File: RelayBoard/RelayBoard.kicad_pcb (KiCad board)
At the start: 2 copper layers, 96.3 x 38.1 mm, 63 parts, among them J1 Micro_SD_Card, J10 Conn_01x04_Male, J11 Conn_01x04_Male, J12 Conn_01x04_Male, J2 Screw_Terminal_01x02, J3 Conn_01x04_Male, J4 Conn_01x04_Male, J5 Conn_01x04_Male, J6 Conn_01x04_Male, J7 SI-52008-F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

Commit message: add jlcjlcjlcjlc
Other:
- board text added: "JLCJLCJLCJLC"
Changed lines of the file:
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@@
   (general
     (thickness 1.6)
-    (drawings 10)
+    (drawings 11)
     (tracks 705)
     (zones 0)
@@
       (outputformat 1)
       (mirror false)
-      (drillshape 1)
+      (drillshape 0)
       (scaleselection 1)
       (outputdirectory ""))
@@
     )
   )
+  (gr_text JLCJLCJLCJLC (at 97.79 80.264 -90) (layer F.SilkS)
+    (effects (font (size 1 1) (thickness 0.15)))
+  )
   (gr_text "Relay Board v1 by Clive Chan" (at 167.64 97.282) (layer F.SilkS)

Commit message: Programming connector, CAN connectors 2.54mm
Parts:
- removed J12, J6: Conn_01x04_Male, Connector_PinHeader_1.00mm:PinHeader_1x04_P1.00mm_Vertical
- removed the REF** at (130.6, 94.0)
- removed the REF** at (130.6, 67.6)
- added J13: Conn_01x04_Male, Connector_PinHeader_2.54mm:PinHeader_1x04_P2.54mm_Vertical, F.Cu at (150.4, 82.8)
- added REF**: MountingHole_3.2mm_M3_Pad_Via, MountingHole:MountingHole_3.2mm_M3_Pad_Via, F.Cu at (130.6, 93.7)
- added REF**: MountingHole_3.2mm_M3_Pad_Via, MountingHole:MountingHole_3.2mm_M3_Pad_Via, F.Cu at (130.6, 67.3)
- G***: moved to B.Cu
- J10, J11, J3, J4, J5, J9: footprint Connector_PinHeader_1.00mm:PinHeader_1x04_P1.00mm_Vertical -> Connector_JST:JST_XH_B4B-XH-AM_1x04_P2.50mm_Vertical
- moved G*** 90.5 mm to (94.2, 80.0), turned to 270 degrees
- moved J9 27.1 mm to (156.5, 88.6), turned to 270 degrees
- moved U4 25.3 mm to (165.6, 67.3), turned to 180 degrees
- moved J5 17.4 mm to (169.9, 96.3), turned to 180 degrees
- moved D2 13.6 mm to (169.2, 82.0), turned to 0 degrees
- moved J3 12.7 mm to (164.1, 74.7), turned to 270 degrees
- moved J4 10.2 mm to (169.9, 89.4), turned to 180 degrees
- moved U3 8.76 mm to (145.3, 88.6)
- moved J11 7.78 mm to (183.4, 96.3)
- moved JP1 7.06 mm to (169.2, 75.4), turned to 90 degrees
- moved FB2 6.25 mm to (146.8, 93.2)
- moved C14 6.11 mm to (148.6, 96.8)
- moved C11 6.02 mm to (145.0, 93.2)
- moved C12 5.86 mm to (146.8, 96.8)
- moved C7 5.80 mm to (143.3, 93.2)
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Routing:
- net Net-(D2-Pad1): track 27.6 -> 62.3 mm
- net 5V_CAN: track 31.5 -> 63.3 mm, vias 0 -> 1
- net CANL: track 69.5 -> 92.2 mm
- net SWCLK: track 0.00 -> 18.2 mm, vias 0 -> 1
- net 5V: track 75.1 -> 91.5 mm, vias 2 -> 0
- net Net-(C2-Pad2): track 11.2 -> 22.2 mm
- net SWDIO: track 0.00 -> 9.81 mm
- net SD_CMD: track 41.7 -> 49.6 mm
- net VDDA_3.3: track 29.0 -> 21.1 mm, vias 0 -> 2
- net CANH: track 61.8 -> 68.8 mm
- net 3V3: track 219.4 -> 215.6 mm, vias 3 -> 5
- net CANTX: track 18.3 -> 14.5 mm
- net SD_D3: track 43.9 -> 47.5 mm
- net SD_D0: track 40.3 -> 43.8 mm
- net 24V: track 79.2 -> 82.6 mm
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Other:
- outline, holes or cut-outs redrawn
- board text added: "Relay Board v1.1 by Clive Chan"
- board text removed: "Relay Board v1 by Clive Chan"

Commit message: replace pin jumper with solder jumper
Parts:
- removed JP1: Jumper_NO_Small, Jumper:SolderJumper-2_P1.3mm_Open_Pad1.0x1.5mm
- added R15: 0Ω, Resistor_SMD:R_0805_2012Metric_Pad1.15x1.40mm_HandSolder, F.Cu at (169.4, 76.2)
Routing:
- net 5V_CAN: track 63.3 -> 65.0 mm

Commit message: better solder jumper pad
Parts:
- R15: footprint Resistor_SMD:R_0805_2012Metric_Pad1.15x1.40mm_HandSolder -> Jumper:SolderJumper-2_P1.3mm_Open_TrianglePad1.0x1.5mm
- moved R15 1.30 mm to (169.2, 74.9)
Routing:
- net 5V_CAN: track 65.0 -> 62.4 mm
- net 5V: track 91.7 -> 90.9 mm
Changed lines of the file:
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@@
     (thickness 1.6)
     (drawings 10)
-    (tracks 829)
+    (tracks 831)
     (zones 0)
     (modules 62)
@@
     (add_net VDDC)
   )
-  (module Resistor_SMD:R_0805_2012Metric_Pad1.15x1.40mm_HandSolder (layer F.Cu)
-    (at 169.418 76.2 270)
-    (descr "Resistor SMD 0805 (2012 Metric), square (rectangular) end terminal, IPC_7351 nominal with elongated pad for handsoldering. (Body size source: https://docs.google.com/spreadsheets/d/1BsfQQcO9C6DZCsRaXUlFlo91Tg2WpOkGARC1WS5S8t0/edit?usp=sharing), generated with kicad-footprint-generator")
-    (tags "resistor handsolder")
-    (attr smd)
-    (fp_text reference R15 (at 0 -1.65 90) (layer F.SilkS)
+  (module Jumper:SolderJumper-2_P1.3mm_Open_TrianglePad1.0x1.5mm (layer F.Cu)
+    (at 169.164 74.93 270)
+    (descr "SMD Solder Jumper, 1x1.5mm Triangular Pads, 0.3mm gap, open")
+    (tags "solder jumper open")
+    (attr virtual)
+    (fp_text reference R15 (at 0 -1.8 90) (layer F.SilkS)
       (effects (font (size 1 1) (thickness 0.15)))
     )
-    (fp_text value 0Ω (at 0 1.65 90) (layer F.Fab)
+    (fp_text value 0Ω (at 0 1.9 90) (layer F.Fab)
       (effects (font (size 1 1) (thickness 0.15)))
     )
-    (fp_text user %R (at 0 0 90) (layer F.Fab)
-      (effects (font (size 0.5 0.5) (thickness 0.08)))
-    )
-    (fp_line (start 1.85 0.95) (end -1.85 0.95) (layer F.CrtYd) (width 0.05))
-    (fp_line (start 1.85 -0.95) (end 1.85 0.95) (layer F.CrtYd) (width 0.05))
-    (fp_line (start -1.85 -0.95) (end 1.85 -0.95) (layer F.CrtYd) (width 0.05))
-    (fp_line (start -1.85 0.95) (end -1.85 -0.95) (layer F.CrtYd) (width 0.05))
-    (fp_line (start -0.261252 0.71) (end 0.261252 0.71) (layer F.SilkS) (width 0.12))
-    (fp_line (start -0.261252 -0.71) (end 0.261252 -0.71) (layer F.SilkS) (width 0.12))
-    (fp_line (start 1 0.6) (end -1 0.6) (layer F.Fab) (width 0.1))
-    (fp_line (start 1 -0.6) (end 1 0.6) (layer F.Fab) (width 0.1))
-    (fp_line (start -1 -0.6) (end 1 -0.6) (layer F.Fab) (width 0.1))
-    (fp_line (start -1 0.6) (end -1 -0.6) (layer F.Fab) (width 0.1))
-    (pad 2 smd roundrect (at 1.025 0 270) (size 1.15 1.4) (layers F.Cu F.Paste F.Mask) (roundrect_rratio 0.217391)
-      (net 72 5V_CAN))
-    (pad 1 smd roundrect (at -1.025 0 270) (size 1.15 1.4) (layers F.Cu F.Paste F.Mask) (roundrect_rratio 0.217391)
-      (net 24 5V))
-    (model ${KISYS3DMOD}/Resistor_SMD.3dshapes/R_0805_2012Metric.wrl
-      (at (xyz 0 0 0))
-      (scale (xyz 1 1 1))
-      (rotate (xyz 0 0 0))
-    )
+    (fp_line (start 1.65 1.25) (end -1.65 1.25) (layer F.CrtYd) (width 0.05))
+    (fp_line (start 1.65 1.25) (end 1.65 -1.25) (layer F.CrtYd) (width 0.05))
+    (fp_line (start -1.65 -1.25) (end -1.65 1.25) (layer F.CrtYd) (width 0.05))
+    (fp_line (start -1.65 -1.25) (end 1.65 -1.25) (layer F.CrtYd) (width 0.05))
+    (fp_line (start -1.4 -1) (end 1.4 -1) (layer F.SilkS) (width 0.12))
+    (fp_line (start 1.4 -1) (end 1.4 1) (layer F.SilkS) (width 0.12))
+    (fp_line (start 1.4 1) (end -1.4 1) (layer F.SilkS) (width 0.12))
+    (fp_line (start -1.4 1) (end -1.4 -1) (layer F.SilkS) (width 0.12))
+    (pad 1 smd custom (at -0.725 0 270) (size 0.3 0.3) (layers F.Cu F.Mask)
+      (net 24 5V) (zone_connect 2)
+      (options (clearance outline) (anchor rect))
+      (primitives
+        (gr_poly (pts
+           (xy -0.5 -0.75) (xy 0.5 -0.75) (xy 1 0) (xy 0.5 0.75) (xy -0.5 0.75)
+) (width 0))
+      ))
+    (pad 2 smd custom (at 0.725 0 270) (size 0.3 0.3) (layers F.Cu F.Mask)
+      (net 72 5V_CAN) (zone_connect 2)
+      (options (clearance outline) (anchor rect))
+      (primitives
+        (gr_poly (pts
+           (xy -0.65 -0.75) (xy 0.5 -0.75) (xy 0.5 0.75) (xy -0.65 0.75) (xy -0.15 0)
+) (width 0))
+      ))
   )
   (module Waterloop:waterloop-logo (layer B.Cu)
@@
   (segment (start 150.983998 82.804) (end 152.283999 84.104001) (width 0.5) (layer F.Cu) (net 24) (status 10))
   (segment (start 150.368 82.804) (end 150.983998 82.804) (width 0.5) (layer F.Cu) (net 24) (status 30))
-  (segment (start 169.808 74.785) (end 169.418 75.175) (width 0.5) (layer F.Cu) (net 24) (status 30))
-  (segment (start 169.808 69.59) (end 169.808 74.785) (width 0.5) (layer F.Cu) (net 24) (status 30))
+  (segment (start 169.808 73.561) (end 169.164 74.205) (width 0.5) (layer F.Cu) (net 24))
+  (segment (start 169.808 69.59) (end 169.808 73.561) (width 0.5) (layer F.Cu) (net 24))
   (via (at 117.856 74.168) (size 0.8) (drill 0.4) (layers F.Cu B.Cu) (net 25))
   (segment (start 119.013 74.168) (end 117.856 74.168) (width 0.25) (layer F.Cu) (net 25) (status 10))
@@
   (segment (start 167.858011 63.760046) (end 167.858011 65.550049) (width 0.5) (layer F.Cu) (net 71))
   (via (at 166.624 82.042) (size 0.8) (drill 0.4) (layers F.Cu B.Cu) (net 72))
-  (segment (start 165.496 76.088) (end 164.084 74.676) (width 0.5) (layer F.Cu) (net 72) (status 20))
   (segment (start 169.926 89.408) (end 169.926 96.266) (width 0.5) (layer F.Cu) (net 72) (status 30))
   (segment (start 183.388 96.266) (end 183.388 89.408) (width 0.5) (layer F.Cu) (net 72) (status 30))
@@
   (segment (start 167.113999 82.531999) (end 167.113999 86.124001) (width 0.5) (layer B.Cu) (net 72))
   (segment (start 167.113999 86.124001) (end 167.113999 86.595999) (width 0.5) (layer B.Cu) (net 72))
-  (segment (start 166.633 77.225) (end 169.418 77.225) (width 0.5) (layer F.Cu) (net 72) (status 20))
-  (segment (start 164.084 74.676) (end 166.633 77.225) (width 0.5) (layer F.Cu) (net 72) (status 10))
-  (segment (start 166.624 80.019) (end 166.624 82.042) (width 0.5) (layer F.Cu) (net 72))
-  (segment (start 169.418 77.225) (end 166.624 80.019) (width 0.5) (layer F.Cu) (net 72) (status 10))
+  (segment (start 166.624 78.195) (end 166.624 82.042) (width 0.5) (layer F.Cu) (net 72))
+  (segment (start 165.063 75.655) (end 164.084 74.676) (width 0.5) (layer F.Cu) (net 72))
+  (segment (start 165.063 75.655) (end 167.1135 77.7055) (width 0.5) (layer F.Cu) (net 72))
+  (segment (start 167.1135 77.7055) (end 166.624 78.195) (width 0.5) (layer F.Cu) (net 72))
+  (segment (start 167.1135 77.7055) (end 167.6585 77.7055) (width 0.5) (layer F.Cu) (net 72))
+  (segment (start 167.6585 77.7055) (end 169.164 76.2) (width 0.5) (layer F.Cu) (net 72))
+  (segment (start 169.164 76.2) (end 169.164 75.955) (width 0.5) (layer F.Cu) (net 72))
   (via (at 146.304 76.2) (size 0.8) (drill 0.4) (layers F.Cu B.Cu) (net 73))
   (segment (start 154.272999 83.979001) (end 155.448 82.804) (width 0.25) (layer B.Cu) (net 73) (status 20))

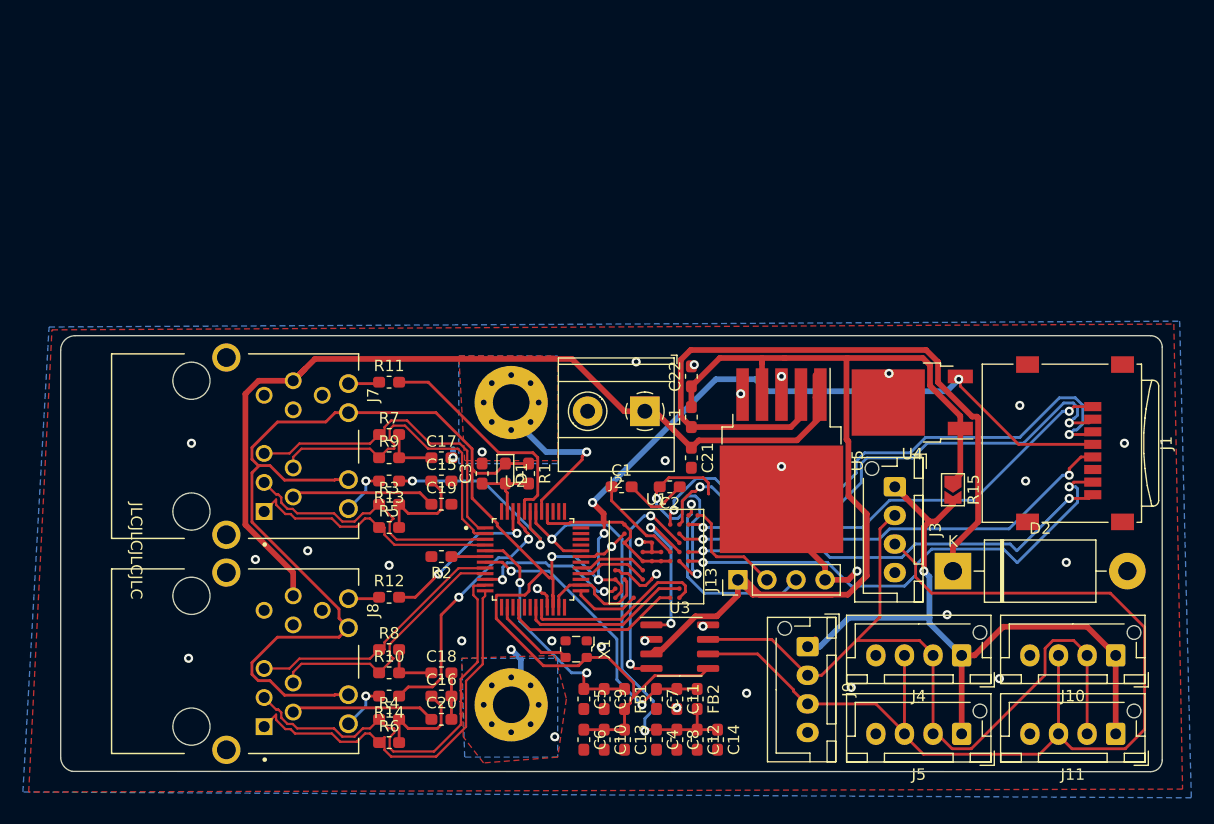
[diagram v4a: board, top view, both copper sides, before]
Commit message: substantial rewiring after adding MDIO and MCL
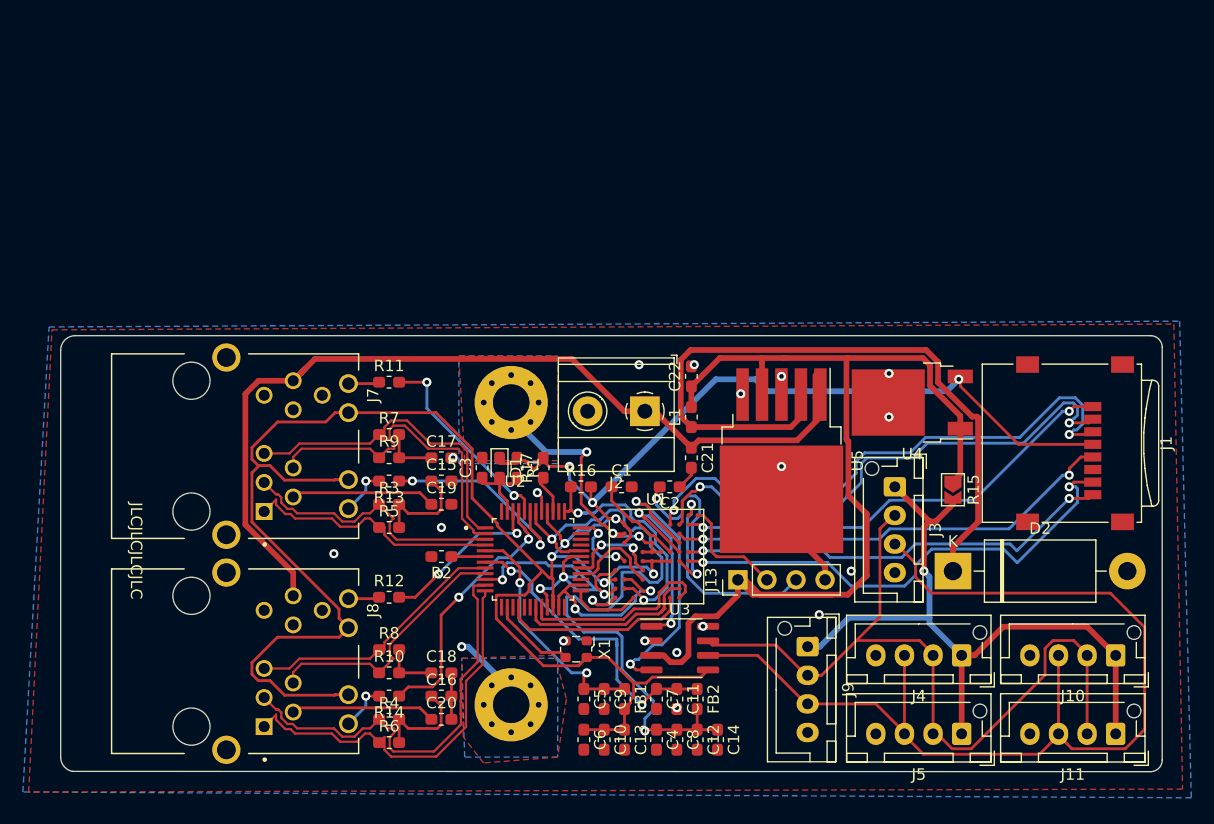
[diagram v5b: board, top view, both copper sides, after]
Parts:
- added R16: 4.7kΩ, Resistor_SMD:R_0603_1608Metric_Pad1.05x0.95mm_HandSolder, F.Cu at (136.7, 74.7)
- added R17: 4.7kΩ, Resistor_SMD:R_0603_1608Metric_Pad1.05x0.95mm_HandSolder, F.Cu at (133.3, 73.0)
- moved R1 1.14 mm to (131.1, 73.0)
- moved D1 0.72 mm to (129.5, 73.0)
- moved C3 0.51 mm to (128.0, 73.0)
- moved U3 0.13 mm to (145.3, 88.8)
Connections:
- U2 pad 36: Net-(U2-Pad36) -> MDC
- U2 pad 37: Net-(U2-Pad37) -> MDIO
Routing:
- net MDIO: track 0.00 -> 22.3 mm, vias 0 -> 2
- net VDDC: track 39.5 -> 58.6 mm
- net 3V3: track 215.6 -> 229.7 mm, vias 5 -> 9
- net CANRX: track 19.5 -> 29.1 mm
- net GND: track 73.8 -> 81.2 mm, vias 38 -> 26
- net MDC: track 0.00 -> 6.38 mm, vias 0 -> 2
- net REF_CLK: track 10.1 -> 16.0 mm, vias 0 -> 2
- net Net-(C2-Pad2): track 22.2 -> 16.5 mm
- net CANTX: track 14.5 -> 18.0 mm
- net Net-(R17-Pad1): track 0.00 -> 2.90 mm
- net P1LED1: track 20.5 -> 17.6 mm, vias 0 -> 2
- net RXD0: track 6.13 -> 8.66 mm, vias 0 -> 2
- net 5V: track 90.9 -> 93.1 mm
- net TXD1: track 15.1 -> 17.2 mm
- net RXD1: track 6.29 -> 8.26 mm
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
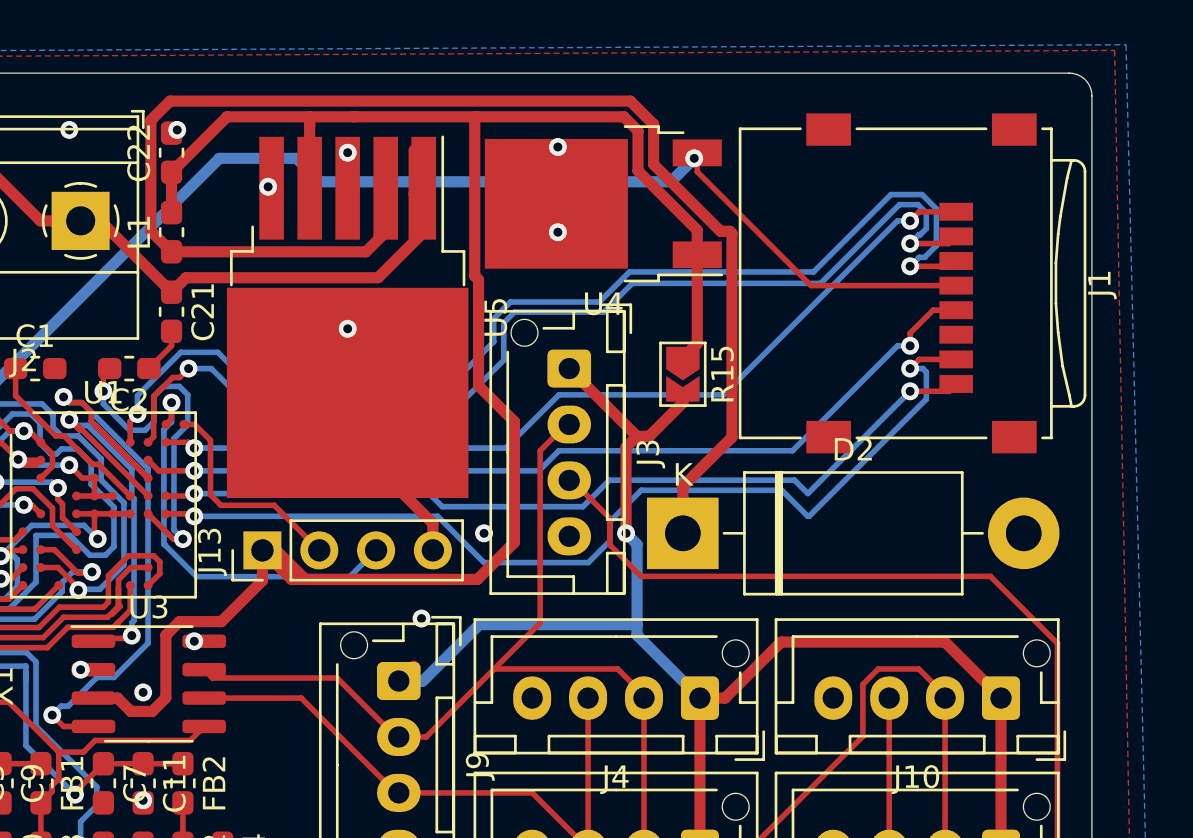
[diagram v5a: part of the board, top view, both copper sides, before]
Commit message: add polyfuse, check all RMII stuff, shorten diode trace
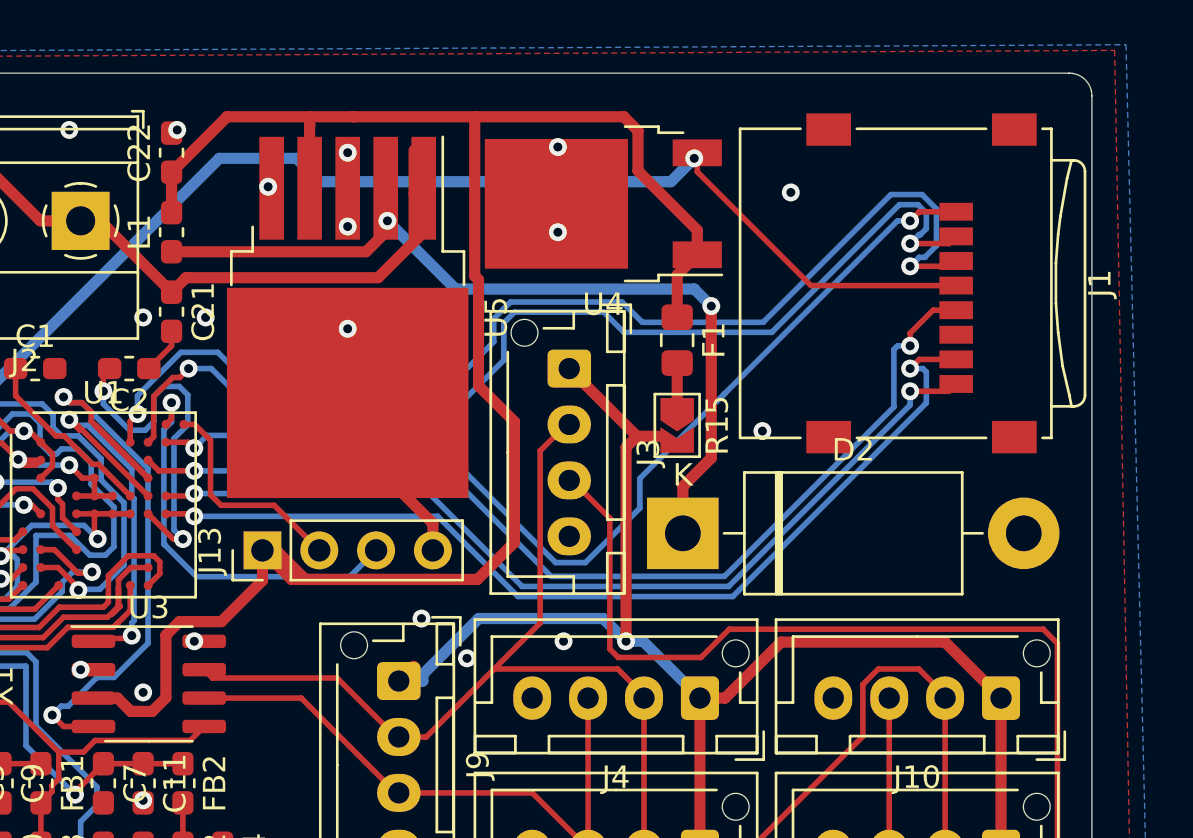
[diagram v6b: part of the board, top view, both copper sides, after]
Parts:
- added F1: 1A, Fuse:Fuse_0805_2012Metric_Pad1.15x1.40mm_HandSolder, F.Cu at (168.9, 73.4)
- moved R15 2.30 mm to (168.9, 77.2)
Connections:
- R15 pad 1: 5V -> Net-(F1-Pad2)
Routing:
- net Net-(D2-Pad1): track 62.3 -> 38.6 mm, vias 0 -> 2
- net SD_D2: track 40.1 -> 45.7 mm
- net SD_CLK: track 39.6 -> 45.0 mm
- net CANL: track 92.0 -> 95.8 mm
- net SD_D1: track 38.5 -> 41.3 mm
- net Net-(F1-Pad2): track 0.00 -> 2.06 mm
- net 5V: track 93.1 -> 91.3 mm
- net 5V_CAN: track 62.4 -> 61.6 mm
- net SD_D3: track 47.5 -> 48.3 mm
- net SD_CMD: track 49.6 -> 50.3 mm
- net GND: vias 26 -> 32

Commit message: partial rework of power - needs some bigger components oops
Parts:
- added C23: 470uF EMZS350ARA471MHA0G, Capacitor_SMD:CP_Elec_10x10, B.Cu at (161.5, 40.1)
- added L2: 22uH PA4320, Inductor_SMD:L_Pulse_PA4320, B.Cu at (162.1, 52.6)
- C21: value 100uF -> 470uF EMZS350ARA471MHA0G; footprint Capacitor_SMD:C_0603_1608Metric_Pad1.05x0.95mm_HandSolder -> Capacitor_SMD:CP_Elec_10x10; moved to B.Cu
- C22: value 330uF -> 330uF EMZS350ARA331MHA0G; footprint Capacitor_SMD:C_0603_1608Metric_Pad1.05x0.95mm_HandSolder -> Capacitor_SMD:CP_Elec_10x10; moved to B.Cu
- D2: value 1N5822 -> CCS15F40L3FTR-ND; footprint Diode_THT:D_DO-201AD_P15.24mm_Horizontal -> Diode_SMD:D_0603_1608Metric_Pad1.05x0.95mm_HandSolder
- L1: value 330uH -> 330uH PA4320; footprint Inductor_SMD:L_0603_1608Metric_Pad1.05x0.95mm_HandSolder -> Inductor_SMD:L_Pulse_PA4320; moved to B.Cu
- moved C21 35.1 mm to (130.3, 40.9), turned to 90 degrees
- moved D2 26.5 mm to (146.3, 68.6), turned to 270 degrees
- moved C22 25.0 mm to (148.6, 40.1)
- moved L1 16.1 mm to (148.1, 52.6), turned to 0 degrees
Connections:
- C22 pad 1: 5V -> Net-(C22-Pad1)
- L1 pad 2: 5V -> Net-(C22-Pad1)
- U5 pad 4: 5V -> Net-(C22-Pad1)
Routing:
- net Net-(D2-Pad1): track 38.6 -> 14.2 mm, vias 2 -> 1
- net 5V: track 91.3 -> 72.0 mm
- net GND: track 81.2 -> 88.5 mm, vias 32 -> 31
